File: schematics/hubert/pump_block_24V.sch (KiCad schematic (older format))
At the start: 11 parts, among them M5 PUMP24V, U4 L6205N

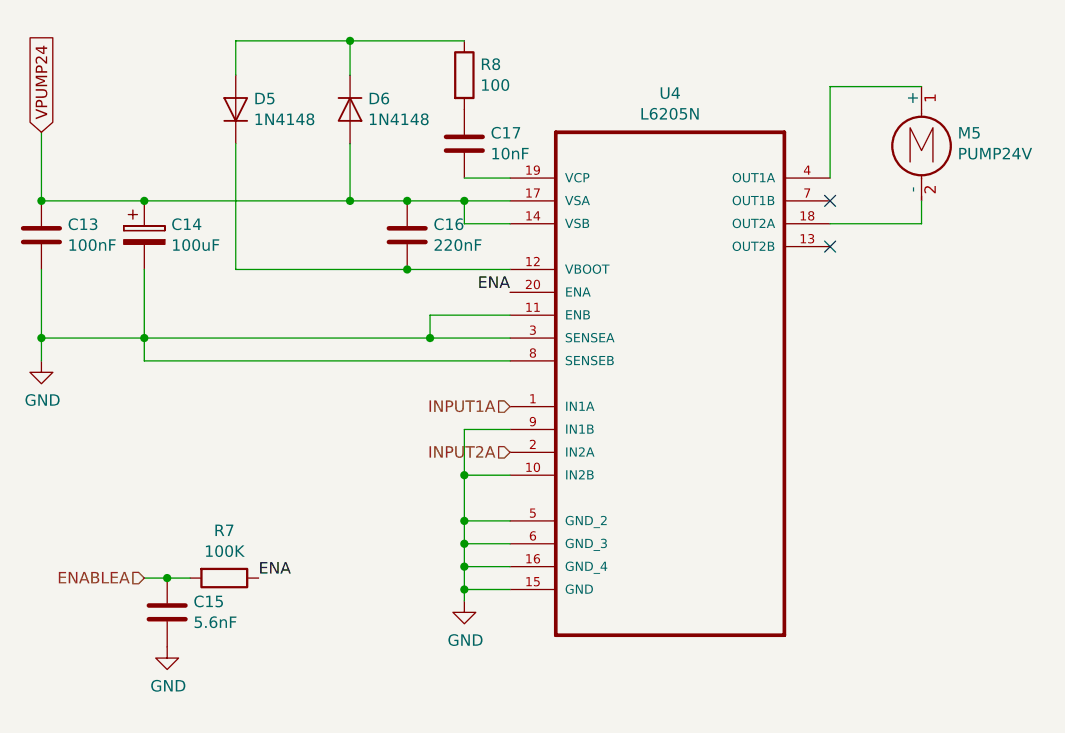
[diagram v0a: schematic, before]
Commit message: updated schematics
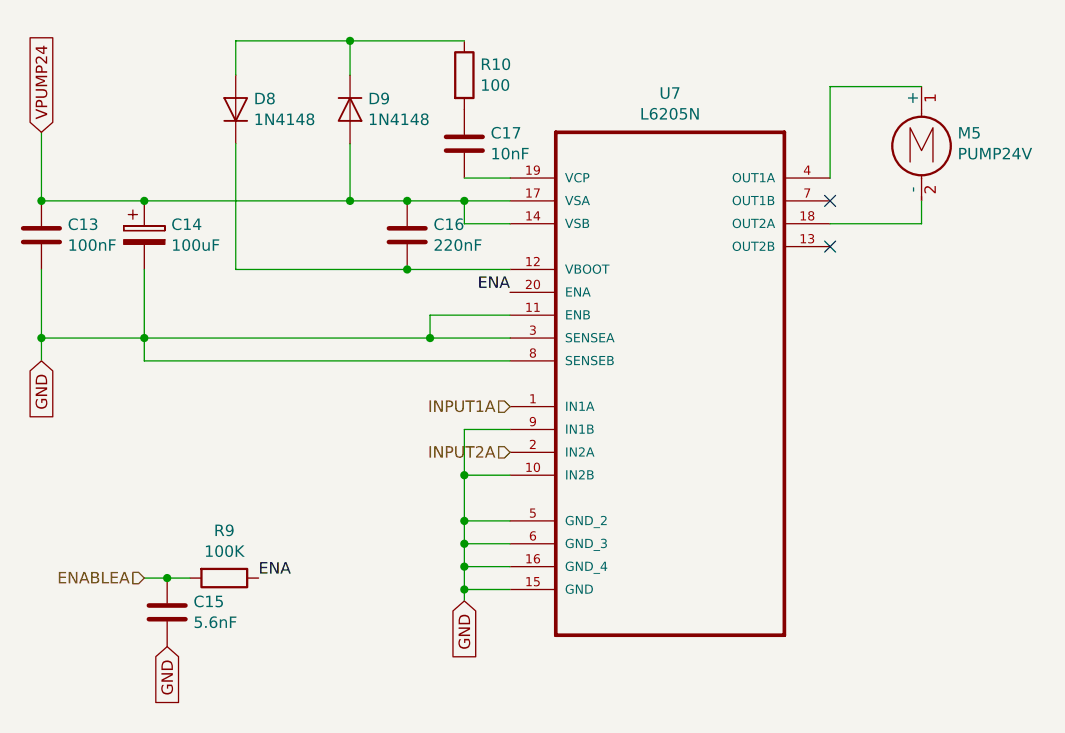
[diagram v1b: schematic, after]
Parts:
- renumbered D5 to D8, D6 to D9, R8 to R10, R7 to R9, U4 to U7
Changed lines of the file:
@@
 $Descr A4 11693 8268
 encoding utf-8
-Sheet 4 6
+Sheet 4 7
 Title "Hubert"
-Date "2018-10-31"
-Rev "1"
+Date "2018-11-02"
+Rev "1.1"
 Comp ""
 Comment1 ""
@@
 AR Path="/5BDA8753/5BDB4D6C" Ref="U?"  Part="1"
 AR Path="/5BDAC3DF/5BDB4D6C" Ref="U?"  Part="1"
-AR Path="/5BDAC585/5BDB4D6C" Ref="U4"  Part="1"
-F 0 "U4" H 6800 4270 50  0000 C CNN
+AR Path="/5BDAC585/5BDB4D6C" Ref="U7"  Part="1"
+F 0 "U7" H 6800 4270 50  0000 C CNN
 F 1 "L6205N" H 6800 4179 50  0000 C CNN
 F 2 "DIP254P762X510-20" H 6800 3100 50  0001 L BNN
@@
 	1    0    0    -1
 $EndComp
-$Comp
-L power:GND #PWR?
-U 1 1 5BDB4D6D
-P 5900 4150
-AR Path="/5BDB4D6D" Ref="#PWR?"  Part="1"
-AR Path="/5BDA8753/5BDB4D6D" Ref="#PWR?"  Part="1"
-AR Path="/5BDAC3DF/5BDB4D6D" Ref="#PWR?"  Part="1"
-AR Path="/5BDAC585/5BDB4D6D" Ref="#PWR014"  Part="1"
-F 0 "#PWR014" H 5900 3900 50  0001 C CNN
-F 1 "GND" H 5905 3977 50  0000 C CNN
-F 2 "" H 5900 4150 50  0001 C CNN
-F 3 "" H 5900 4150 50  0001 C CNN
-	1    5900 4150
-	1    0    0    -1
-$EndComp
 Wire Wire Line
 	5900 4150 5900 4100
@@
 AR Path="/5BDA8753/5BDAA856" Ref="D?"  Part="1"
 AR Path="/5BDAC3DF/5BDAA856" Ref="D?"  Part="1"
-AR Path="/5BDAC585/5BDAA856" Ref="D6"  Part="1"
-F 0 "D6" V 5354 2079 50  0000 L CNN
+AR Path="/5BDAC585/5BDAA856" Ref="D9"  Part="1"
+F 0 "D9" V 5354 2079 50  0000 L CNN
 F 1 "1N4148" V 5445 2079 50  0000 L CNN
 F 2 "Diode_THT:D_DO-35_SOD27_P7.62mm_Horizontal" H 5400 1825 50  0001 C CNN
@@
 AR Path="/5BDA8753/5BDAA866" Ref="R?"  Part="1"
 AR Path="/5BDAC3DF/5BDAA866" Ref="R?"  Part="1"
-AR Path="/5BDAC585/5BDAA866" Ref="R8"  Part="1"
-F 0 "R8" H 5970 1896 50  0000 L CNN
+AR Path="/5BDAC585/5BDAA866" Ref="R10"  Part="1"
+F 0 "R10" H 5970 1896 50  0000 L CNN
 F 1 "100" H 5970 1805 50  0000 L CNN
 F 2 "" V 5830 1850 50  0001 C CNN
@@
 AR Path="/5BDA8753/5BDAA873" Ref="D?"  Part="1"
 AR Path="/5BDAC3DF/5BDAA873" Ref="D?"  Part="1"
-AR Path="/5BDAC585/5BDAA873" Ref="D5"  Part="1"
-F 0 "D5" V 4946 1921 50  0000 R CNN
+AR Path="/5BDAC585/5BDAA873" Ref="D8"  Part="1"
+F 0 "D8" V 4946 1921 50  0000 R CNN
 F 1 "1N4148" V 4855 1921 50  0000 R CNN
 F 2 "Diode_THT:D_DO-35_SOD27_P7.62mm_Horizontal" H 4900 1825 50  0001 C CNN
@@
 $EndComp
 Connection ~ 4050 2400
-$Comp
-L power:GND #PWR?
-U 1 1 5BDAA89B
-P 4050 3100
-AR Path="/5BDAA89B" Ref="#PWR?"  Part="1"
-AR Path="/5BDA8753/5BDAA89B" Ref="#PWR?"  Part="1"
-AR Path="/5BDAC3DF/5BDAA89B" Ref="#PWR?"  Part="1"
-AR Path="/5BDAC585/5BDAA89B" Ref="#PWR012"  Part="1"
-F 0 "#PWR012" H 4050 2850 50  0001 C CNN
-F 1 "GND" H 4055 2927 50  0000 C CNN
-F 2 "" H 4050 3100 50  0001 C CNN
-F 3 "" H 4050 3100 50  0001 C CNN
-	1    4050 3100
-	1    0    0    -1
-$EndComp
 Wire Wire Line
 	4050 2700 4050 3000
@@
 $EndComp
 $Comp
-L power:GND #PWR?
-U 1 1 5BDAA8B8
-P 4600 4350
-AR Path="/5BDAA8B8" Ref="#PWR?"  Part="1"
-AR Path="/5BDA8753/5BDAA8B8" Ref="#PWR?"  Part="1"
-AR Path="/5BDAC3DF/5BDAA8B8" Ref="#PWR?"  Part="1"
-AR Path="/5BDAC585/5BDAA8B8" Ref="#PWR013"  Part="1"
-F 0 "#PWR013" H 4600 4100 50  0001 C CNN
-F 1 "GND" H 4605 4177 50  0000 C CNN
-F 2 "" H 4600 4350 50  0001 C CNN
-F 3 "" H 4600 4350 50  0001 C CNN
-	1    4600 4350
-	1    0    0    -1
-$EndComp
-$Comp
 L Device:R R?
 U 1 1 5BDAA8C4
@@
 AR Path="/5BDA8753/5BDAA8C4" Ref="R?"  Part="1"
 AR Path="/5BDAC3DF/5BDAA8C4" Ref="R?"  Part="1"
-AR Path="/5BDAC585/5BDAA8C4" Ref="R7"  Part="1"
-F 0 "R7" V 4643 4050 50  0000 C CNN
+AR Path="/5BDAC585/5BDAA8C4" Ref="R9"  Part="1"
+F 0 "R9" V 4643 4050 50  0000 C CNN
 F 1 "100K" V 4734 4050 50  0000 C CNN
 F 2 "" V 4780 4050 50  0001 C CNN
@@
 Text GLabel 4050 2100 1    50   Input ~ 0
 VPUMP24
+Text GLabel 4600 4350 3    50   Input ~ 0
+GND
+Text GLabel 4050 3100 3    50   Input ~ 0
+GND
+Text GLabel 5900 4150 3    50   Input ~ 0
+GND
 $EndSCHEMATC

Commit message: fixed ERC problems and added connector for input pins
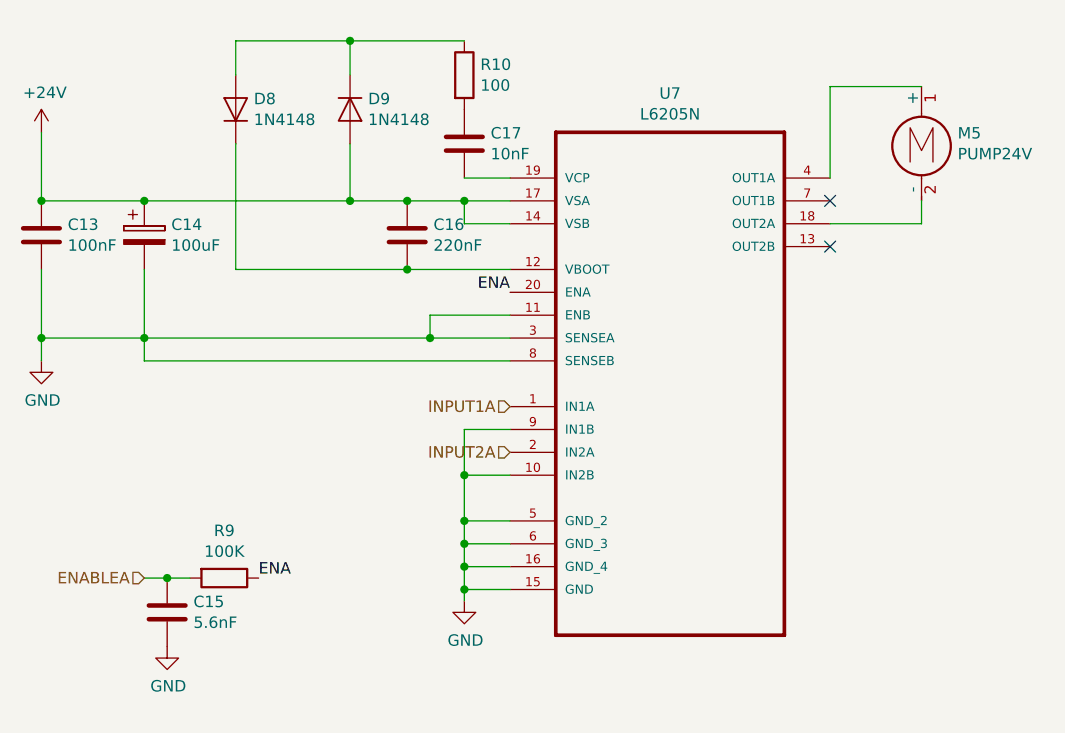
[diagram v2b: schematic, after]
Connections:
- net VPUMP24 renamed +24V
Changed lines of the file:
@@
 NoConn ~ 7500 2400
 NoConn ~ 7500 2600
-Text GLabel 4050 2100 1    50   Input ~ 0
-VPUMP24
-Text GLabel 4600 4350 3    50   Input ~ 0
-GND
-Text GLabel 4050 3100 3    50   Input ~ 0
-GND
-Text GLabel 5900 4150 3    50   Input ~ 0
-GND
+$Comp
+L power:+24V #PWR0117
+U 1 1 5BE29EA3
+P 4050 2100
+F 0 "#PWR0117" H 4050 1950 50  0001 C CNN
+F 1 "+24V" H 4065 2273 50  0000 C CNN
+F 2 "" H 4050 2100 50  0001 C CNN
+F 3 "" H 4050 2100 50  0001 C CNN
+	1    4050 2100
+	1    0    0    -1
+$EndComp
+$Comp
+L power:GND #PWR0118
+U 1 1 5BE29F02
+P 4050 3100
+F 0 "#PWR0118" H 4050 2850 50  0001 C CNN
+F 1 "GND" H 4055 2927 50  0000 C CNN
+F 2 "" H 4050 3100 50  0001 C CNN
+F 3 "" H 4050 3100 50  0001 C CNN
+	1    4050 3100
+	1    0    0    -1
+$EndComp
+$Comp
+L power:GND #PWR0119
+U 1 1 5BE2A314
+P 4600 4350
+F 0 "#PWR0119" H 4600 4100 50  0001 C CNN
+F 1 "GND" H 4605 4177 50  0000 C CNN
+F 2 "" H 4600 4350 50  0001 C CNN
+F 3 "" H 4600 4350 50  0001 C CNN
+	1    4600 4350
+	1    0    0    -1
+$EndComp
+$Comp
+L power:GND #PWR0120
+U 1 1 5BE2A335
+P 5900 4150
+F 0 "#PWR0120" H 5900 3900 50  0001 C CNN
+F 1 "GND" H 5905 3977 50  0000 C CNN
+F 2 "" H 5900 4150 50  0001 C CNN
+F 3 "" H 5900 4150 50  0001 C CNN
+	1    5900 4150
+	1    0    0    -1
+$EndComp
 $EndSCHEMATC

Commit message: started working on layout
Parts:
- C13, C15, C16, C17: footprint (none) -> Capacitor_THT:CP_Radial_D5.0mm_P2.50mm
- C14: footprint (none) -> Capacitor_THT:CP_Radial_D6.3mm_P2.50mm
- R10, R9: footprint (none) -> Resistor_THT:R_Axial_DIN0617_L17.0mm_D6.0mm_P25.40mm_Horizontal
- U7: footprint DIP254P762X510-20 -> Package_DIP:DIP-20_W7.62mm_Socket
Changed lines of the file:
@@
 Sheet 4 7
 Title "Hubert"
-Date "2018-11-02"
-Rev "1.1"
+Date "2018-11-05"
+Rev "1.2"
 Comp ""
 Comment1 ""
@@
 F 0 "U7" H 6800 4270 50  0000 C CNN
 F 1 "L6205N" H 6800 4179 50  0000 C CNN
-F 2 "DIP254P762X510-20" H 6800 3100 50  0001 L BNN
+F 2 "Package_DIP:DIP-20_W7.62mm_Socket" H 6800 3100 50  0001 L BNN
 F 3 "L6205N" H 6800 3100 50  0001 L BNN
 F 4 "Unavailable" H 6800 3100 50  0001 L BNN "Field4"
@@
 F 0 "C17" H 6015 2196 50  0000 L CNN
 F 1 "10nF" H 6015 2105 50  0000 L CNN
-F 2 "" H 5938 2000 50  0001 C CNN
+F 2 "Capacitor_THT:CP_Radial_D5.0mm_P2.50mm" H 5938 2000 50  0001 C CNN
 F 3 "~" H 5900 2150 50  0001 C CNN
 	1    5900 2150
@@
 F 0 "R10" H 5970 1896 50  0000 L CNN
 F 1 "100" H 5970 1805 50  0000 L CNN
-F 2 "" V 5830 1850 50  0001 C CNN
+F 2 "Resistor_THT:R_Axial_DIN0617_L17.0mm_D6.0mm_P25.40mm_Horizontal" V 5830 1850 50  0001 C CNN
 F 3 "~" H 5900 1850 50  0001 C CNN
 	1    5900 1850
@@
 F 0 "C16" H 5765 2596 50  0000 L CNN
 F 1 "220nF" H 5765 2505 50  0000 L CNN
-F 2 "" H 5688 2400 50  0001 C CNN
+F 2 "Capacitor_THT:CP_Radial_D5.0mm_P2.50mm" H 5688 2400 50  0001 C CNN
 F 3 "~" H 5650 2550 50  0001 C CNN
 	1    5650 2550
@@
 F 0 "C14" H 4618 2596 50  0000 L CNN
 F 1 "100uF" H 4618 2505 50  0000 L CNN
-F 2 "" H 4538 2400 50  0001 C CNN
+F 2 "Capacitor_THT:CP_Radial_D6.3mm_P2.50mm" H 4538 2400 50  0001 C CNN
 F 3 "~" H 4500 2550 50  0001 C CNN
 	1    4500 2550
@@
 F 0 "C13" H 4165 2596 50  0000 L CNN
 F 1 "100nF" H 4165 2505 50  0000 L CNN
-F 2 "" H 4088 2400 50  0001 C CNN
+F 2 "Capacitor_THT:CP_Radial_D5.0mm_P2.50mm" H 4088 2400 50  0001 C CNN
 F 3 "~" H 4050 2550 50  0001 C CNN
 	1    4050 2550
@@
 F 0 "C15" H 4715 4246 50  0000 L CNN
 F 1 "5.6nF" H 4715 4155 50  0000 L CNN
-F 2 "" H 4638 4050 50  0001 C CNN
+F 2 "Capacitor_THT:CP_Radial_D5.0mm_P2.50mm" H 4638 4050 50  0001 C CNN
 F 3 "~" H 4600 4200 50  0001 C CNN
 	1    4600 4200
@@
 F 0 "R9" V 4643 4050 50  0000 C CNN
 F 1 "100K" V 4734 4050 50  0000 C CNN
-F 2 "" V 4780 4050 50  0001 C CNN
+F 2 "Resistor_THT:R_Axial_DIN0617_L17.0mm_D6.0mm_P25.40mm_Horizontal" V 4780 4050 50  0001 C CNN
 F 3 "~" H 4850 4050 50  0001 C CNN
 	1    4850 4050
